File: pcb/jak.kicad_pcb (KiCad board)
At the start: 2 copper layers, 230.5 x 96.9 mm, 92 parts, among them SW1 SW_Push, SW10 SW_Push, SW10_r1 SW_Push, SW11 SW_Push, SW11_r1 SW_Push, SW12 SW_Push, SW12_r1 SW_Push, SW13 SW_Push, SW13_r1 SW_Push, SW14 SW_Push, SW14_r1 SW_Push, SW15 SW_Push, SW15_r1 SW_Push, SW16 SW_Push, SW16_r1 SW_Push, SW17 SW_Push, SW17_r1 SW_Push, SW18 SW_Push, SW18_r1 SW_Push, SW1_r1 SW_Push, SW2 SW_Push, SW2_r1 SW_Push, SW3 SW_Push, SW3_r1 SW_Push, SW4 SW_Push, SW4_r1 SW_Push, SW5 SW_Push, SW5_r1 SW_Push, SW6 SW_Push, SW6_r1 SW_Push, SW7 SW_Push, SW7_r1 SW_Push, SW8 SW_Push, SW8_r1 SW_Push, SW9 SW_Push, SW9_r1 SW_Push

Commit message: Modified the pcb to have stronger mousebites
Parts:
- removed the REF** at (147.6, 120.0)
- removed the REF** at (147.6, 103.0)
- added REF**: MouseBite-Slot_2.0x4.5mm_inset_D0.5mm_P0.85mm_7h, Panelization:MouseBite-Slot_2.0x4.5mm_inset_D0.5mm_P0.85mm_7h, F.Cu at (146.0, 116.8)
- added REF**: MouseBite-Slot_2.0x4.5mm_inset_D0.5mm_P0.85mm_7h, Panelization:MouseBite-Slot_2.0x4.5mm_inset_D0.5mm_P0.85mm_7h, F.Cu at (146.0, 97.7)
- added REF**: MouseBite-Slot_2.0x4.5mm_inset_D0.5mm_P0.85mm_7h, Panelization:MouseBite-Slot_2.0x4.5mm_inset_D0.5mm_P0.85mm_7h, F.Cu at (146.0, 78.7)
- moved SW11_r1 117.9 mm to (134.4, 116.8)
- moved SW1_r1 117.9 mm to (134.4, 78.7)
- moved SW6_r1 117.9 mm to (134.4, 97.7)
- moved D21 117.9 mm to (102.2, 60.7)
- moved D26 117.9 mm to (102.2, 79.7)
- moved D31 117.9 mm to (102.2, 98.8)
- moved H5 117.9 mm to (124.9, 76.2)
- moved SW14_r1 117.9 mm to (77.3, 104.3)
- moved SW4_r1 117.9 mm to (77.3, 66.2)
- moved SW9_r1 117.9 mm to (77.3, 85.2)
- moved controller_r1 117.9 mm to (39.2, 92.8)
- moved D19 117.9 mm to (140.3, 78.7)
- moved D20 117.9 mm to (121.2, 66.7)
- moved D22 117.9 mm to (83.1, 66.2)
- moved D23 117.9 mm to (64.1, 68.7)
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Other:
- board size 230.5 x 96.9 mm -> 230.3 x 96.9 mm

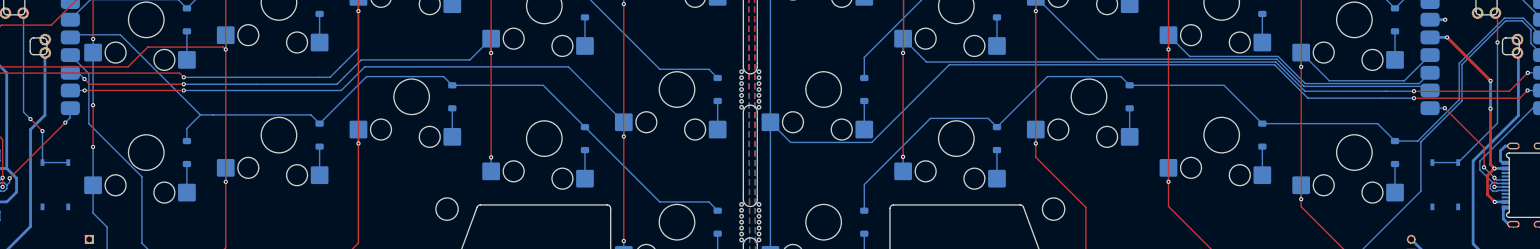
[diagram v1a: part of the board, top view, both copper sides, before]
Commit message: Fixed the footprint for the reset switch, as it was wrong on the website I got it from
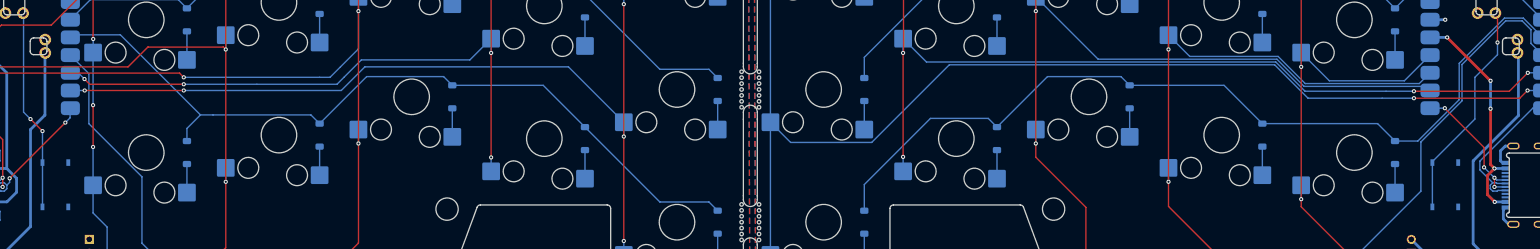
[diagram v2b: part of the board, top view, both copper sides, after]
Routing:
- net reset: track 27.2 -> 31.3 mm
- net reset_r: track 25.8 -> 28.4 mm
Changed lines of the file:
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@@
 			(layer "B.Fab")
 		)
+		(fp_text user "PCB Edge"
+			(at 6.46 -1.49 270)
+			(layer "B.Fab")
+			(effects
+				(font
+					(size 0.64 0.64)
+					(thickness 0.15)
+				)
+				(justify mirror)
+			)
+		)
 		(pad "A1_B12" smd rect
 			(at -3.2 5.15 90)
@@
 			(layer "B.Fab")
 		)
+		(fp_text user "*"
+			(at -3.434349 3.5518 270)
+			(unlocked yes)
+			(layer "B.SilkS")
+			(effects
+				(font
+					(size 1 1)
+					(thickness 0.15)
+				)
+				(justify mirror)
+			)
+		)
+		(fp_text user "*"
+			(at -3.434349 3.5518 270)
+			(layer "B.SilkS")
+			(effects
+				(font
+					(size 1 1)
+					(thickness 0.15)
+				)
+				(justify mirror)
+			)
+		)
+		(fp_text user "*"
+			(at -2.3241 2.6289 270)
+			(unlocked yes)
+			(layer "B.Fab")
+			(effects
+				(font
+					(size 1 1)
+					(thickness 0.15)
+				)
+				(justify mirror)
+			)
+		)
+		(fp_text user "*"
+			(at -2.3241 2.6289 270)
+			(layer "B.Fab")
+			(effects
+				(font
+					(size 1 1)
+					(thickness 0.15)
+				)
+				(justify mirror)
+			)
+		)
 		(fp_text user "${REFERENCE}"
 			(at 0 0 270)
@@
 		)
 		(pad "2" smd rect
-			(at -3.180349 -1.849999 90)
+			(at 3.180349 1.849999 90)
 			(size 0.9505 0.5588)
 			(layers "B.Cu" "B.Mask" "B.Paste")
@@
 		)
 		(pad "3" smd rect
-			(at 3.180349 -1.849999 90)
+			(at -3.180349 -1.849999 90)
 			(size 0.9505 0.5588)
 			(layers "B.Cu" "B.Mask" "B.Paste")
@@
 		)
 		(pad "4" smd rect
-			(at 3.180349 1.849999 90)
+			(at 3.180349 -1.849999 90)
 			(size 0.9505 0.5588)
 			(layers "B.Cu" "B.Mask" "B.Paste")
@@
 			(layer "B.Fab")
 		)
+		(fp_text user "*"
+			(at -3.434349 3.5518 90)
+			(layer "B.SilkS")
+			(effects
+				(font
+					(size 1 1)
+					(thickness 0.15)
+				)
+				(justify mirror)
+			)
+		)
+		(fp_text user "*"
+			(at -3.434349 3.5518 90)
+			(unlocked yes)
+			(layer "B.SilkS")
+			(effects
+				(font
+					(size 1 1)
+					(thickness 0.15)
+				)
+				(justify mirror)
+			)
+		)
 		(fp_text user "${REFERENCE}"
 			(at 0 0 90)
@@
 			)
 		)
+		(fp_text user "*"
+			(at -2.3241 2.6289 90)
+			(unlocked yes)
+			(layer "B.Fab")
+			(effects
+				(font
+					(size 1 1)
+					(thickness 0.15)
+				)
+				(justify mirror)
+			)
+		)
+		(fp_text user "*"
+			(at -2.3241 2.6289 90)
+			(layer "B.Fab")
+			(effects
+				(font
+					(size 1 1)
+					(thickness 0.15)
+				)
+				(justify mirror)
+			)
+		)
 		(pad "1" smd rect
 			(at -3.180349 1.849999 270)
@@
 		)
 		(pad "2" smd rect
-			(at -3.180349 -1.849999 270)
+			(at 3.180349 1.849999 270)
 			(size 0.9505 0.5588)
 			(layers "B.Cu" "B.Mask" "B.Paste")
@@
 		)
 		(pad "3" smd rect
-			(at 3.180349 -1.849999 270)
+			(at -3.180349 -1.849999 270)
 			(size 0.9505 0.5588)
 			(layers "B.Cu" "B.Mask" "B.Paste")
@@
 		)
 		(pad "4" smd rect
-			(at 3.180349 1.849999 270)
+			(at 3.180349 -1.849999 270)
 			(size 0.9505 0.5588)
 			(layers "B.Cu" "B.Mask" "B.Paste")
@@
 	)
 	(segment
-		(start 246.600554 108.241926)
-		(end 252.250555 102.591925)
+		(start 249 96)
+		(end 249 102)
+		(width 0.2)
+		(layer "B.Cu")
+		(net 13)
+	)
+	(segment
+		(start 249 102)
+		(end 242.900556 108.099444)
+		(width 0.2)
+		(layer "B.Cu")
+		(net 13)
+	)
+	(segment
+		(start 252.250555 92.749445)
+		(end 249 96)
 		(width 0.2)
 		(layer "B.Cu")
@@
 	(segment
 		(start 242.900556 108.241926)
-		(end 246.600554 108.241926)
+		(end 242.900556 114.602624)
 		(width 0.2)
 		(layer "B.Cu")
@@
 	)
 	(segment
-		(start 252.250555 102.591925)
-		(end 252.250555 91)
+		(start 252.250555 91)
+		(end 252.250555 92.749445)
+		(width 0.2)
+		(layer "B.Cu")
+		(net 13)
+	)
+	(segment
+		(start 242.900556 108.099444)
+		(end 242.900556 108.241926)
 		(width 0.2)
 		(layer "B.Cu")
@@
 	)
 	(segment
-		(start 40.631055 101)
-		(end 40.631055 87.309237)
+		(start 43.350055 103.719)
+		(end 43.350055 108.241926)
 		(width 0.2)
 		(layer "B.Cu")
@@
 	)
 	(segment
-		(start 43.350055 103.719)
-		(end 43.350055 108.241926)
+		(start 40.631055 101)
+		(end 40.631055 87.309237)
 		(width 0.2)
 		(layer "B.Cu")
@@
 	)
 	(segment
-		(start 41.631055 102)
-		(end 40.631055 101)
+		(start 43.350055 114.602624)
+		(end 43.350055 108.241926)
 		(width 0.2)
 		(layer "B.Cu")
@@
 	)
 	(segment
-		(start 47.050053 108.241926)
-		(end 43.350055 108.241926)
+		(start 41.631055 102)
+		(end 40.631055 101)
 		(width 0.2)
 		(layer "B.Cu")

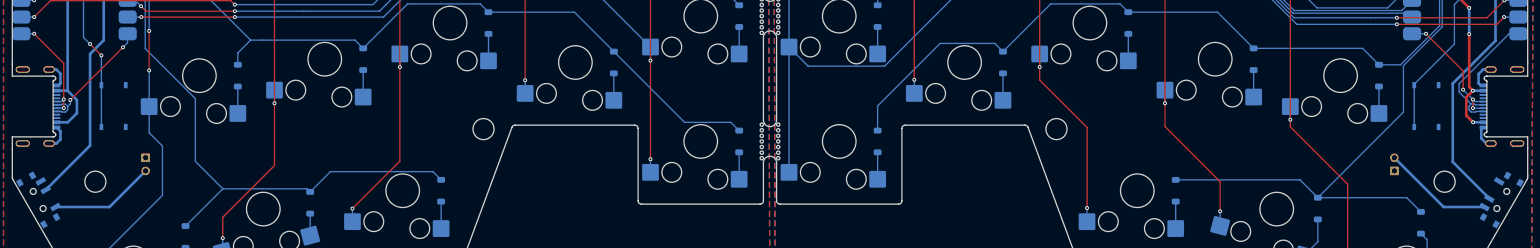
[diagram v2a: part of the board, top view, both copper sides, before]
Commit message: Fixed the power switch pins being swapped and updated the gerber files
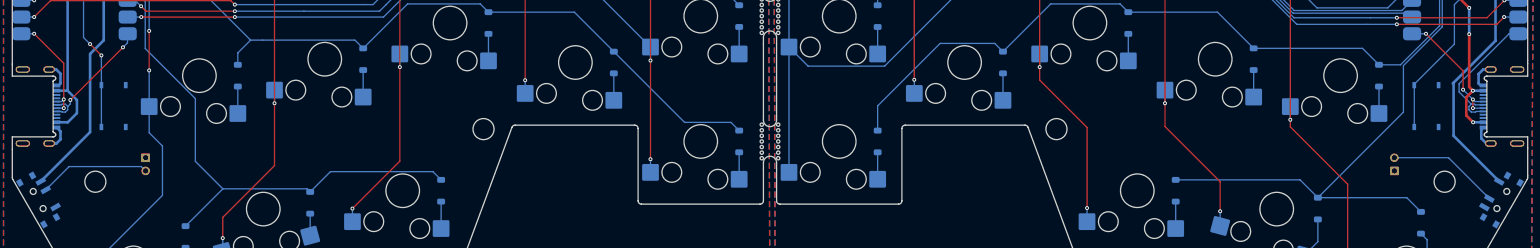
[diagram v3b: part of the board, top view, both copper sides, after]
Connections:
- power1 pad 1: unconnected-(power1-A-Pad1) -> battery_switched
- power1 pad 2: battery_switched -> battery+
- power1 pad 3: battery+ -> unconnected-(power1-C-Pad3)
- power_r1 pad 1: battery+_r -> unconnected-(power_r1-A-Pad1)
- power_r1 pad 2: battery_switched_r -> battery+_r
- power_r1 pad 3: unconnected-(power_r1-C-Pad3) -> battery_switched_r
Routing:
- net battery_switched: track 37.3 -> 35.4 mm
- net battery_switched_r: track 34.6 -> 33.7 mm
- net battery+_r: track 16.0 -> 16.9 mm
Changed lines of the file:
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@@
 	(net 21 "col4_r")
 	(net 22 "battery_switched_r")
-	(net 23 "unconnected-(power_r1-C-Pad3)")
+	(net 23 "unconnected-(power1-C-Pad3)")
 	(net 24 "col2_r")
 	(net 25 "row2_r")
@@
 	(net 65 "Net-(D35-A)")
 	(net 66 "Net-(D36-A)")
-	(net 67 "unconnected-(power1-A-Pad1)")
+	(net 67 "unconnected-(power_r1-A-Pad1)")
 	(net 68 "split_comms-")
 	(net 69 "split_comms+")
@@
 			(size 0.7 1.5)
 			(layers "B.Cu" "B.Mask" "B.Paste")
-			(net 2 "battery+_r")
+			(net 67 "unconnected-(power_r1-A-Pad1)")
 			(pinfunction "A")
-			(pintype "passive")
+			(pintype "passive+no_connect")
 		)
 		(pad "2" smd rect
@@
 			(size 0.7 1.5)
 			(layers "B.Cu" "B.Mask" "B.Paste")
-			(net 22 "battery_switched_r")
+			(net 2 "battery+_r")
 			(pinfunction "B")
 			(pintype "passive")
@@
 			(size 0.7 1.5)
 			(layers "B.Cu" "B.Mask" "B.Paste")
-			(net 23 "unconnected-(power_r1-C-Pad3)")
+			(net 22 "battery_switched_r")
 			(pinfunction "C")
-			(pintype "passive+no_connect")
+			(pintype "passive")
 		)
 		(embedded_fonts no)
@@
 			(size 0.7 1.5)
 			(layers "B.Cu" "B.Mask" "B.Paste")
-			(net 67 "unconnected-(power1-A-Pad1)")
+			(net 12 "battery_switched")
 			(pinfunction "A")
-			(pintype "passive+no_connect")
+			(pintype "passive")
 		)
 		(pad "2" smd rect
@@
 			(size 0.7 1.5)
 			(layers "B.Cu" "B.Mask" "B.Paste")
-			(net 12 "battery_switched")
+			(net 1 "battery+")
 			(pinfunction "B")
 			(pintype "passive")
@@
 			(size 0.7 1.5)
 			(layers "B.Cu" "B.Mask" "B.Paste")
-			(net 1 "battery+")
+			(net 23 "unconnected-(power1-C-Pad3)")
 			(pinfunction "C")
-			(pintype "passive")
+			(pintype "passive+no_connect")
 		)
 		(embedded_fonts no)
@@
 	)
 	(segment
-		(start 253.562139 126.769519)
-		(end 247.370574 126.769519)
-		(width 0.4)
+		(start 239.876055 119.275)
+		(end 248.116658 119.275)
+		(width 0.2)
 		(layer "B.Cu")
 		(net 1)
 	)
 	(segment
-		(start 247.370574 126.769519)
-		(end 239.876055 119.275)
-		(width 0.4)
+		(start 248.116658 119.275)
+		(end 254.312139 125.470481)
+		(width 0.2)
 		(layer "B.Cu")
 		(net 1)
@@
 	(segment
 		(start 50.075055 121.275)
-		(end 44.580536 126.769519)
-		(width 0.4)
+		(end 49.421055 120.621)
+		(width 0.2)
 		(layer "B.Cu")
 		(net 2)
 	)
 	(segment
-		(start 44.580536 126.769519)
-		(end 36.388471 126.769519)
-		(width 0.4)
+		(start 38.438914 120.621)
+		(end 34.888471 124.171443)
+		(width 0.2)
+		(layer "B.Cu")
+		(net 2)
+	)
+	(segment
+		(start 49.421055 120.621)
+		(end 38.438914 120.621)
+		(width 0.2)
 		(layer "B.Cu")
 		(net 2)
@@
 	)
 	(segment
+		(start 248.875277 107.875277)
+		(end 255.250555 101.5)
+		(width 0.4)
+		(layer "B.Cu")
+		(net 12)
+	)
+	(segment
 		(start 255.250555 101.5)
 		(end 255.250555 93.122674)
@@
 	)
 	(segment
-		(start 248.750555 119.908897)
-		(end 248.750555 108)
+		(start 248.875277 107.875277)
+		(end 248.875277 115.935543)
 		(width 0.4)
 		(layer "B.Cu")
@@
 	(segment
 		(start 248.750555 108)
-		(end 255.250555 101.5)
+		(end 248.875277 107.875277)
 		(width 0.4)
 		(layer "B.Cu")
@@
 	)
 	(segment
-		(start 254.312139 125.470481)
-		(end 248.750555 119.908897)
+		(start 248.875277 115.935543)
+		(end 255.812139 122.872405)
 		(width 0.4)
 		(layer "B.Cu")
@@
 	)
 	(segment
+		(start 41.631055 115.379821)
+		(end 34.138471 122.872405)
+		(width 0.4)
+		(layer "B.Cu")
+		(net 22)
+	)
+	(segment
 		(start 43.705055 101.426)
 		(end 43.705055 93.205387)
@@
 	)
 	(segment
-		(start 34.888471 124.171443)
-		(end 41.631055 117.428859)
-		(width 0.4)
-		(layer "B.Cu")
-		(net 22)
-	)
-	(segment
-		(start 41.631055 117.428859)
-		(end 41.631055 103.5)
+		(start 41.631055 103.5)
+		(end 41.631055 115.379821)
 		(width 0.4)
 		(layer "B.Cu")

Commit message: Revert "Fixed the power switch pins being swapped and updated the gerber files"
This reverts commit 317bf88c69a0fc961124c453349158f4046b94f1.
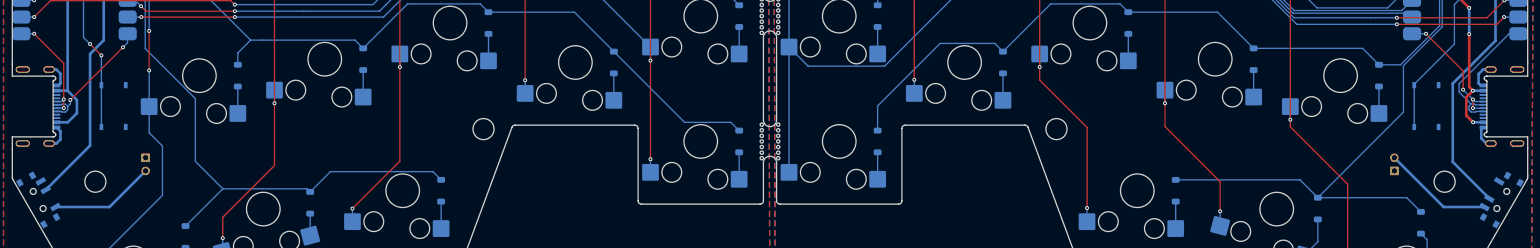
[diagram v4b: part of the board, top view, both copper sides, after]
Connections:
- power1 pad 1: battery_switched -> unconnected-(power1-A-Pad1)
- power1 pad 2: battery+ -> battery_switched
- power1 pad 3: unconnected-(power1-C-Pad3) -> battery+
- power_r1 pad 1: unconnected-(power_r1-A-Pad1) -> battery+_r
- power_r1 pad 2: battery+_r -> battery_switched_r
- power_r1 pad 3: battery_switched_r -> unconnected-(power_r1-C-Pad3)
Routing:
- net battery_switched: track 35.4 -> 37.3 mm
- net battery_switched_r: track 33.7 -> 34.6 mm
- net battery+_r: track 16.9 -> 16.0 mm
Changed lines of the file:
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@@
 	(net 21 "col4_r")
 	(net 22 "battery_switched_r")
-	(net 23 "unconnected-(power1-C-Pad3)")
+	(net 23 "unconnected-(power_r1-C-Pad3)")
 	(net 24 "col2_r")
 	(net 25 "row2_r")
@@
 	(net 65 "Net-(D35-A)")
 	(net 66 "Net-(D36-A)")
-	(net 67 "unconnected-(power_r1-A-Pad1)")
+	(net 67 "unconnected-(power1-A-Pad1)")
 	(net 68 "split_comms-")
 	(net 69 "split_comms+")
@@
 			(size 0.7 1.5)
 			(layers "B.Cu" "B.Mask" "B.Paste")
-			(net 67 "unconnected-(power_r1-A-Pad1)")
+			(net 2 "battery+_r")
 			(pinfunction "A")
-			(pintype "passive+no_connect")
+			(pintype "passive")
 		)
 		(pad "2" smd rect
@@
 			(size 0.7 1.5)
 			(layers "B.Cu" "B.Mask" "B.Paste")
-			(net 2 "battery+_r")
+			(net 22 "battery_switched_r")
 			(pinfunction "B")
 			(pintype "passive")
@@
 			(size 0.7 1.5)
 			(layers "B.Cu" "B.Mask" "B.Paste")
-			(net 22 "battery_switched_r")
+			(net 23 "unconnected-(power_r1-C-Pad3)")
 			(pinfunction "C")
-			(pintype "passive")
+			(pintype "passive+no_connect")
 		)
 		(embedded_fonts no)
@@
 			(size 0.7 1.5)
 			(layers "B.Cu" "B.Mask" "B.Paste")
-			(net 12 "battery_switched")
+			(net 67 "unconnected-(power1-A-Pad1)")
 			(pinfunction "A")
-			(pintype "passive")
+			(pintype "passive+no_connect")
 		)
 		(pad "2" smd rect
@@
 			(size 0.7 1.5)
 			(layers "B.Cu" "B.Mask" "B.Paste")
-			(net 1 "battery+")
+			(net 12 "battery_switched")
 			(pinfunction "B")
 			(pintype "passive")
@@
 			(size 0.7 1.5)
 			(layers "B.Cu" "B.Mask" "B.Paste")
-			(net 23 "unconnected-(power1-C-Pad3)")
+			(net 1 "battery+")
 			(pinfunction "C")
-			(pintype "passive+no_connect")
+			(pintype "passive")
 		)
 		(embedded_fonts no)
@@
 	)
 	(segment
-		(start 239.876055 119.275)
-		(end 248.116658 119.275)
-		(width 0.2)
+		(start 253.562139 126.769519)
+		(end 247.370574 126.769519)
+		(width 0.4)
 		(layer "B.Cu")
 		(net 1)
 	)
 	(segment
-		(start 248.116658 119.275)
-		(end 254.312139 125.470481)
-		(width 0.2)
+		(start 247.370574 126.769519)
+		(end 239.876055 119.275)
+		(width 0.4)
 		(layer "B.Cu")
 		(net 1)
@@
 	(segment
 		(start 50.075055 121.275)
-		(end 49.421055 120.621)
-		(width 0.2)
-		(layer "B.Cu")
-		(net 2)
-	)
-	(segment
-		(start 38.438914 120.621)
-		(end 34.888471 124.171443)
-		(width 0.2)
+		(end 44.580536 126.769519)
+		(width 0.4)
 		(layer "B.Cu")
 		(net 2)
 	)
 	(segment
-		(start 49.421055 120.621)
-		(end 38.438914 120.621)
-		(width 0.2)
+		(start 44.580536 126.769519)
+		(end 36.388471 126.769519)
+		(width 0.4)
 		(layer "B.Cu")
 		(net 2)
@@
 	)
 	(segment
-		(start 248.875277 107.875277)
-		(end 255.250555 101.5)
-		(width 0.4)
-		(layer "B.Cu")
-		(net 12)
-	)
-	(segment
 		(start 255.250555 101.5)
 		(end 255.250555 93.122674)
@@
 	)
 	(segment
-		(start 248.875277 107.875277)
-		(end 248.875277 115.935543)
+		(start 248.750555 119.908897)
+		(end 248.750555 108)
 		(width 0.4)
 		(layer "B.Cu")
@@
 	(segment
 		(start 248.750555 108)
-		(end 248.875277 107.875277)
+		(end 255.250555 101.5)
 		(width 0.4)
 		(layer "B.Cu")
@@
 	)
 	(segment
-		(start 248.875277 115.935543)
-		(end 255.812139 122.872405)
+		(start 254.312139 125.470481)
+		(end 248.750555 119.908897)
 		(width 0.4)
 		(layer "B.Cu")
@@
 	)
 	(segment
-		(start 41.631055 115.379821)
-		(end 34.138471 122.872405)
-		(width 0.4)
-		(layer "B.Cu")
-		(net 22)
-	)
-	(segment
 		(start 43.705055 101.426)
 		(end 43.705055 93.205387)
@@
 	)
 	(segment
-		(start 41.631055 103.5)
-		(end 41.631055 115.379821)
+		(start 34.888471 124.171443)
+		(end 41.631055 117.428859)
+		(width 0.4)
+		(layer "B.Cu")
+		(net 22)
+	)
+	(segment
+		(start 41.631055 117.428859)
+		(end 41.631055 103.5)
 		(width 0.4)
 		(layer "B.Cu")
